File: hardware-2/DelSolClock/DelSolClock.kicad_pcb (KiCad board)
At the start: 2 copper layers, 63.8 x 70.9 mm, 92 parts, among them J1 Conn_01x02_Male, J10 Conn_01x02_Male, J11 Conn_01x08_Male, J2 Conn_01x06, J3 Conn_01x02_Male, J4 Conn_01x02_Male, J5 Conn_01x02_Male, J6 CLOCK_BUTTONS, J7 Conn_01x02_Male, J8 Conn_01x02_Male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

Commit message: more progress on layout. Not done yet.
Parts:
- moved J9 0.27 mm to (17.5, 175.1)
- moved R11 0.27 mm to (61.4, 180.5)
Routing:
- net +12V: track 0.00 -> 131.6 mm
- net /RESET: track 0.00 -> 76.3 mm, vias 0 -> 3
- net GND: track 0.00 -> 69.9 mm, vias 0 -> 43
- net /GPS_RX_MO: track 0.00 -> 56.0 mm, vias 0 -> 2
- net Net-(J11-Pad2): track 0.00 -> 54.4 mm, vias 0 -> 1
- net /GPS_TX_MI: track 0.00 -> 53.7 mm, vias 0 -> 2
- net Net-(J11-Pad3): track 0.00 -> 50.9 mm, vias 0 -> 2
- net /SCL: track 0.00 -> 47.2 mm
- net Net-(J11-Pad4): track 0.00 -> 45.1 mm, vias 0 -> 2
- net /SDA: track 0.00 -> 44.5 mm
- net Net-(C3-Pad1): track 0.00 -> 42.5 mm, vias 0 -> 5
- net /HOUR: track 0.00 -> 41.2 mm, vias 0 -> 1
- net /BUZZER: track 0.00 -> 39.9 mm, vias 0 -> 2
- net /MIN: track 0.00 -> 38.9 mm, vias 0 -> 1
- net /IGN: track 0.00 -> 35.6 mm
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- added copper zone on F.Cu, net GND

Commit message: most of routing complete, still more work to do.
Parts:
- moved R15 3.96 mm to (24.7, 128.9)
- moved R13 1.69 mm to (22.4, 132.7)
- moved J5 0.66 mm to (72.1, 175.7)
- moved TPSDA1 0.55 mm to (56.3, 145.5)
- moved J8 0.53 mm to (21.3, 175.2)
- moved J1 0.50 mm to (62.2, 149.1)
- moved TPSCL1 0.48 mm to (59.7, 145.5)
- moved R9 0.43 mm to (69.3, 176.6)
- moved J3 0.43 mm to (69.1, 171.2)
- moved R16 0.39 mm to (24.7, 132.7)
- moved C1 0.36 mm to (72.6, 168.4)
- moved C9 0.36 mm to (67.0, 180.6)
- moved R31 0.36 mm to (29.8, 166.0)
- moved R29 0.35 mm to (29.8, 157.1)
- moved R30 0.33 mm to (26.1, 165.9)
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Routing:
- net /GPS_RX_MO: track 56.0 -> 60.2 mm
- net Net-(J7-Pad2): track 33.5 -> 35.2 mm
- net +3V3: track 13.4 -> 15.0 mm
- net Net-(R15-Pad1): track 9.71 -> 8.56 mm
- net +5V: track 14.6 -> 15.4 mm
- net Net-(J11-Pad3): track 50.9 -> 51.5 mm

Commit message: added logo, finished layout, ordered board.
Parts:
- added G***: LOGO, LOGO, F.Cu at (45.1, 192.7)
- added G***: LOGO, LOGO, B.Cu at (44.4, 192.6)
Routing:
- net +3V3: track 15.0 -> 182.8 mm, vias 0 -> 2
- net /BATT: track 4.11 -> 72.0 mm, vias 0 -> 3
- net /SCK: track 0.00 -> 47.8 mm, vias 0 -> 2
- net /TRUNK: track 4.07 -> 49.1 mm, vias 0 -> 4
- net /MISO: track 0.00 -> 44.9 mm, vias 0 -> 2
- net /TFT_CS: track 0.00 -> 43.6 mm, vias 0 -> 2
- net /MOSI: track 0.00 -> 40.4 mm, vias 0 -> 2
- net Net-(C9-Pad1): track 1.81 -> 41.8 mm
- net /TFT_POWER: track 0.00 -> 39.3 mm, vias 0 -> 4
- net /WINDOW: track 15.6 -> 54.7 mm, vias 0 -> 5
- net /ROOF: track 15.1 -> 46.5 mm, vias 0 -> 2
- net /LIGHTS: track 33.7 -> 61.9 mm, vias 0 -> 2
- net /TFT_RESET: track 33.0 -> 38.6 mm
- net /TFT_DC: track 19.9 -> 22.7 mm
- net GND: track 69.8 -> 71.7 mm
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
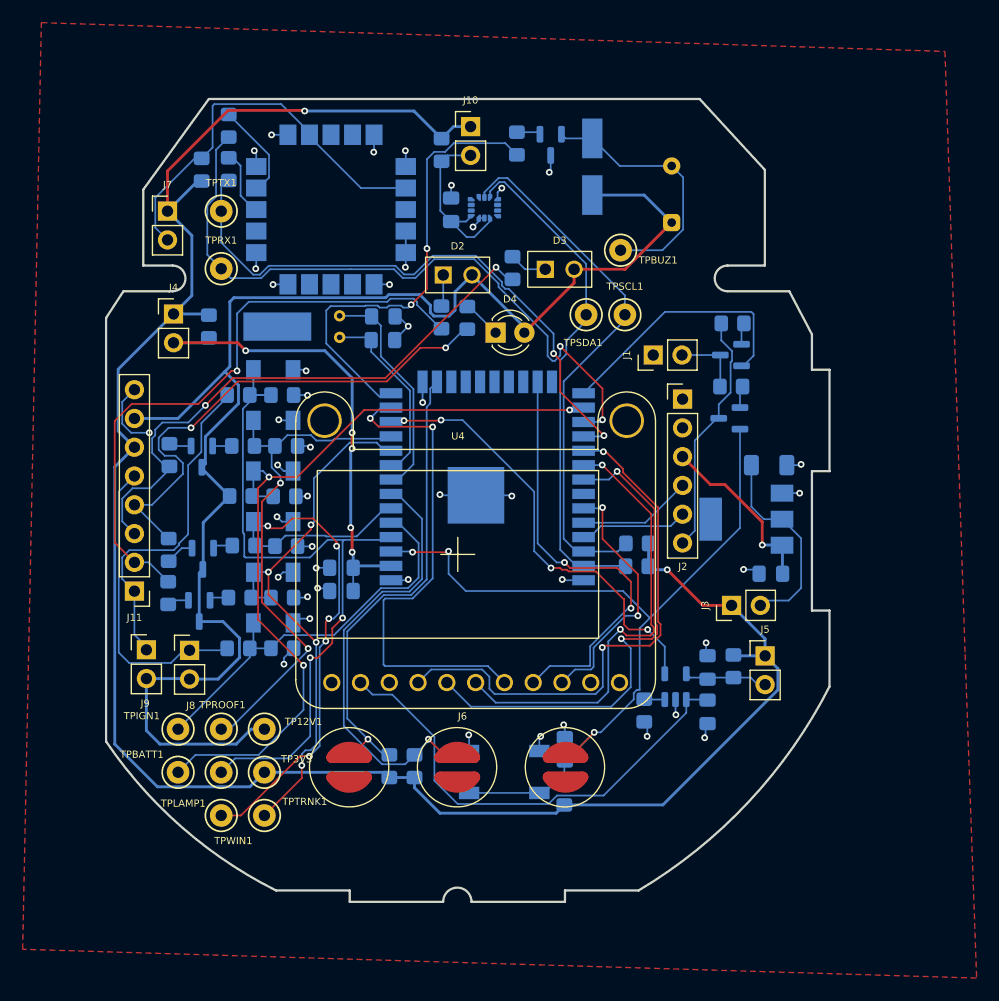
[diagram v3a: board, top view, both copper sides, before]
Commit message: HW updates after testing the last prototype round. fixed PNP and NPN transistor pin mapping error (whoops) added keepouts and moved components inside of the board area. added holes for the rectangle LED footprints added a lot of silkscreen labels
Main remaining item is to adjust LED placement after testing.
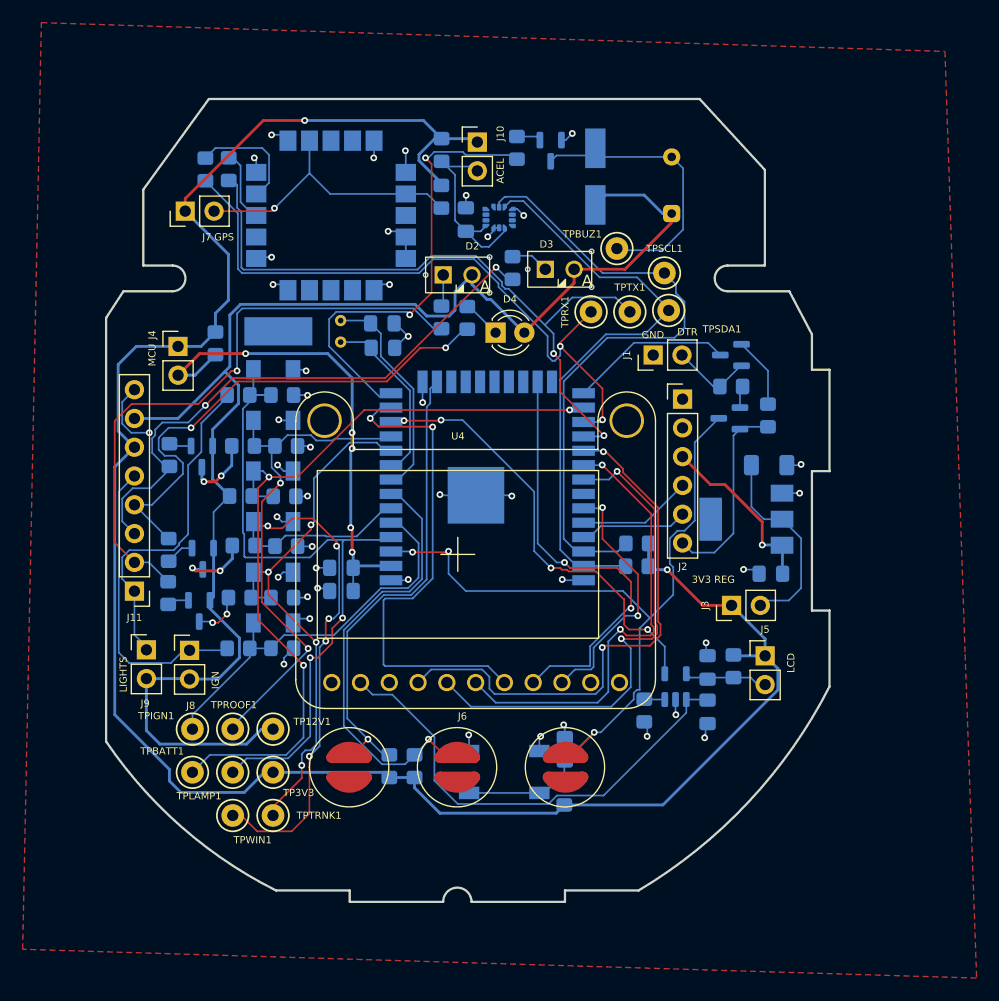
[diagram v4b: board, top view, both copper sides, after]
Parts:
- Q1, Q2, Q3: value PZT2222A -> MMBT2222A
- moved TPTX1 37.1 mm to (60.1, 145.3)
- moved TPRX1 32.9 mm to (56.7, 145.3)
- moved R13 21.3 mm to (43.5, 135.1), turned to -90 degrees
- moved R3 8.71 mm to (72.3, 154.4), turned to 90 degrees
- moved TPSDA1 7.30 mm to (63.6, 145.2)
- moved TPSCL1 5.07 mm to (63.2, 141.9)
- moved R15 4.37 mm to (22.7, 132.7)
- moved J4 2.89 mm to (20.3, 148.3)
- moved R2 1.60 mm to (23.6, 148.1)
- moved J7 1.56 mm to (20.9, 136.4), turned to 90 degrees
- moved C10 1.56 mm to (45.7, 137.1)
- moved U6 1.56 mm to (48.6, 137.0)
- moved J10 1.49 mm to (46.7, 130.3)
- moved TPBATT1 1.27 mm to (21.5, 185.9)
- moved TPIGN1 1.27 mm to (21.5, 182.1)
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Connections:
- Q1 pad 2: /GPIO0 -> /DTR
- Q1 pad 3: /DTR -> /GPIO0
- Q2 pad 2: /RESET -> /RTS
- Q2 pad 3: /RTS -> /RESET
- Q3 pad 2: Net-(BZ1-Pad2) -> GND
- Q3 pad 3: GND -> Net-(BZ1-Pad2)
- Q4 pad 2: /input_divider7/IN -> +12V
- Q4 pad 3: +12V -> /input_divider7/IN
- Q5 pad 2: /input_divider6/IN -> +12V
- Q5 pad 3: +12V -> /input_divider6/IN
- Q6 pad 2: /input_divider5/IN -> +12V
- Q6 pad 3: +12V -> /input_divider5/IN
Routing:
- net Net-(J7-Pad2): track 35.1 -> 25.6 mm, vias 0 -> 1
- net /SCL: track 47.6 -> 56.4 mm
- net /GPIO0: track 23.2 -> 14.6 mm
- net /GPS_TX_MI: track 53.6 -> 61.4 mm
- net /SDA: track 44.9 -> 52.1 mm
- net +12V: track 131.0 -> 126.4 mm
- net /input_divider7/IN: track 1.75 -> 6.20 mm, vias 0 -> 2
- net /input_divider6/IN: track 1.69 -> 6.11 mm, vias 0 -> 2
- net Net-(R3-Pad2): track 1.88 -> 6.25 mm
- net /RTS: track 21.4 -> 17.6 mm
- net /WINDOW: track 54.7 -> 57.8 mm
- net /input_divider5/IN: track 1.73 -> 4.31 mm, vias 0 -> 2
- net /GPS_RX_MO: track 60.2 -> 58.0 mm
- net Net-(R15-Pad1): track 8.56 -> 10.2 mm
- net Net-(C10-Pad1): track 15.4 -> 16.7 mm
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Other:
- board text added: "3V3 REG"
- board text added: "ACEL"
- board text added: "DTR"
- board text added: "GND"
- board text added: "GPS"
- board text added: "IGN"
- board text added: "LCD"
- board text added: "LIGHTS"
- board text added: "MCU"
